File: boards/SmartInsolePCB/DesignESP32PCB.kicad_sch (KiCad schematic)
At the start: 48 parts, among them J1 Conn_01x02_Pin, J10 Conn_01x02_Pin, J11 Conn_01x02_Pin, J12 Conn_01x02_Pin, J2 Conn_01x02_Pin, J3 Conn_01x06_Pin, J4 Conn_01x02_Pin, J5 Conn_01x02_Pin, J6 Conn_01x02_Pin, J7 Conn_01x02_Pin, J8 Conn_01x02_Pin, J9 Conn_01x02_Pin, SW1 SW_Push, SW2 SW_Push, U2 D3V3XA4B10LP, U3 TLV75801PDRV, U6 MPU-6050, U7 ESP32-S3-WROOM-1

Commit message: finished schematic
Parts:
- removed BOOT1, RESET1: ~, Button_Switch_SMD:SW_Push_1P1T_NO_CK_PTS125Sx43PSMTR, symbol Switch:SW_MEC_5E
- removed J3: Conn_01x06_Pin, Connector_PinHeader_1.00mm:PinHeader_1x06_P1.00mm_Vertical, symbol Connector:Conn_01x06_Pin
- added J3: PJS008U-3000-0, SmartInsolePCB:PJS008U30000, symbol SD_Card_Connector:PJS008U-3000-0
- added SW3, SW4: SW_Push, Button_Switch_SMD:SW_Push_1P1T_NO_CK_PTS125Sx43PSMTR, symbol Switch:SW_Push
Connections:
- net GPIO10 is gone; now on net GPIO1: R3.1
- net GPIO13 is gone; now on net GPIO6: R11.1
- net GPIO14 is gone; now on net GPIO7: R12.1
- net GPIO15 is gone; now on net GPIO8: R13.1
- net GPIO16 is gone; now on net GPIO11: R18.1
- net GPIO17 is gone; now on net GPIO12: R19.1
- net GPIO18 is gone; now on net GPIO21: R20.1
- net GPIO19 is gone; now on net GPIO38: R21.1
- net GPIO20 is gone; now on net GPIO47: R22.1
- net SCK is gone; now on net GPIO11: U7.19 (IO11)
- net 3V3: now also J3.4
- net CS: now also U7.21 (IO13), J3.1; no longer U7.20 (IO12)
- net ESP32_EN: now also SW4.2
- net GND: now also J3.3, J3.6, SW3.1, SW4.1
- net GPIO0: now also SW3.2
- net GPIO11: no longer R9.1
- net GPIO12: now also U7.20 (IO12); no longer R10.1
- net MISO: now also U7.8 (IO15), J3.7; no longer U7.22 (IO14)
- net MOSI: now also U7.22 (IO14), J3.2; no longer U7.21 (IO13)
- net GPIO8: now reaches U7.12 (IO8)
- net GPIO3: now reaches U7.15 (IO3)
- net GPIO3: now also R10.1
- net GPIO21: now reaches U7.23 (IO21)
- net GPIO47: now reaches U7.24 (IO47)
- net GPIO38: now reaches U7.31 (IO38)
- net GPIO2: now reaches U7.38 (IO2)
- net GPIO2: now also R9.1
- net GPIO1: now reaches U7.39 (IO1)
- net GPIO6: now reaches U7.6 (IO6)
- net GPIO7: now reaches U7.7 (IO7)
- net SCLK: now reaches U7.9 (IO16)
- net SCLK: now also J3.5
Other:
- note added: "Buttons"
- note added: "ESP32"
- note added: "LDO"
- note added: "MPU 6050"
- note added: "SD Card"
- note added: "USB Connector"
- note added: "Velostat"
- note removed: "Attach to pins going to Velostat material"
- note removed: "Figure out how to interface with I2C and SD card"
- moved on the sheet: C1, C2, C3, C4, J1, J10, J11, J12, J2, J4, J5, J6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

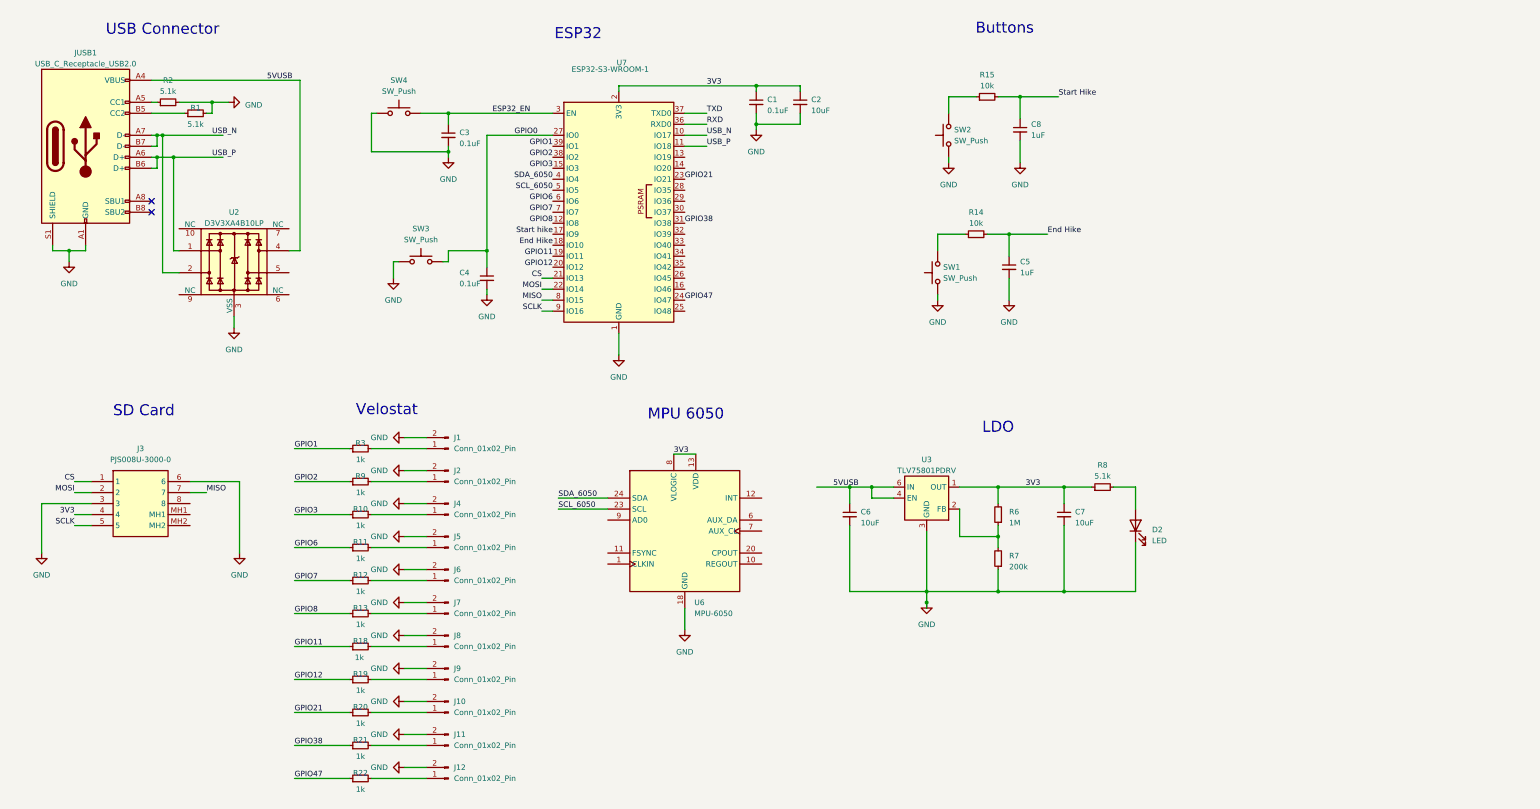
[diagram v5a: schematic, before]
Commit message: finished all PCB connections
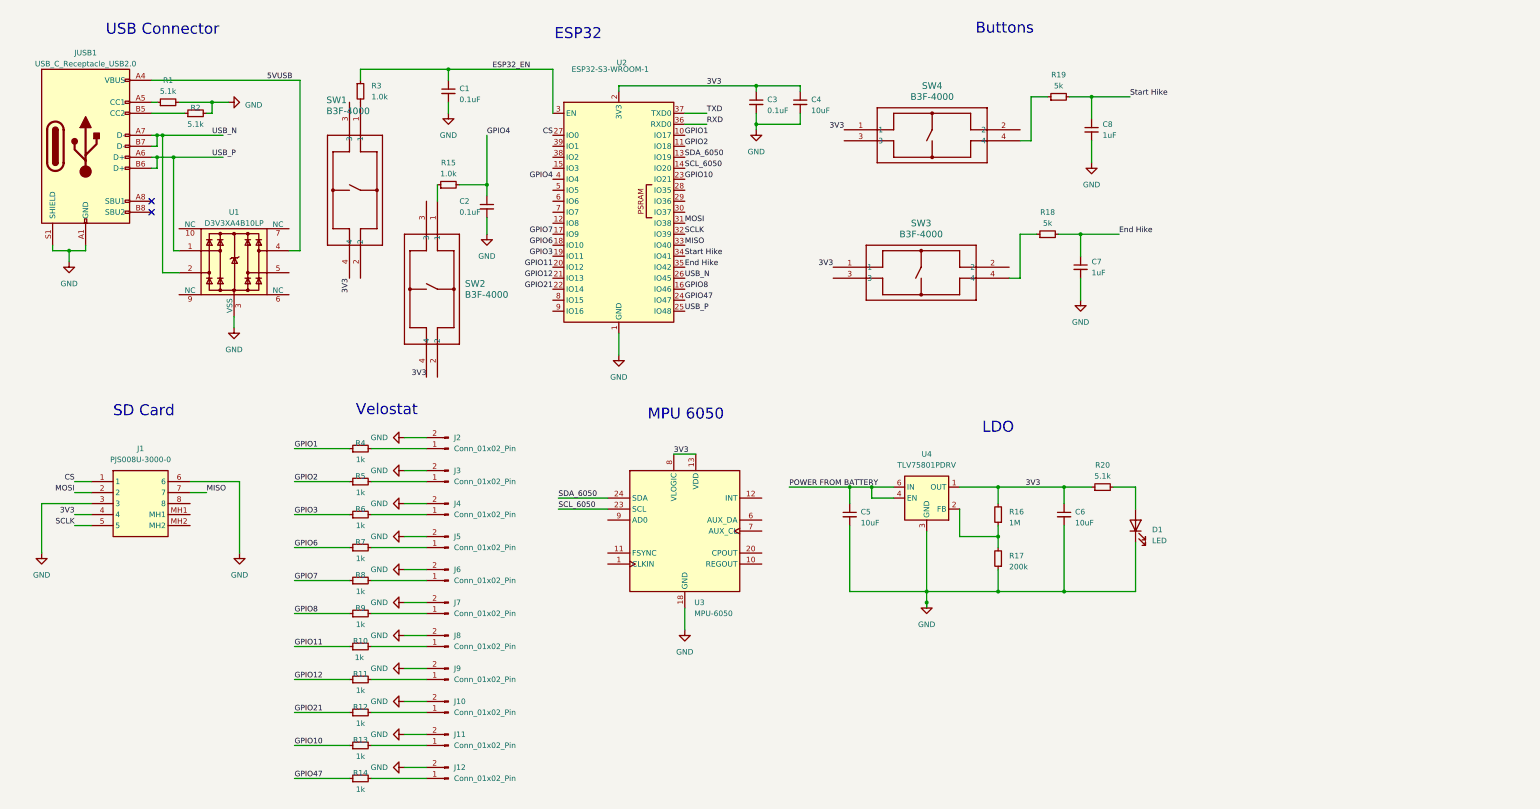
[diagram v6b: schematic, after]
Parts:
- removed SW1, SW2, SW3, SW4: SW_Push, Button_Switch_SMD:SW_Push_1P1T_NO_CK_PTS125Sx43PSMTR, symbol Switch:SW_Push
- added R15, R3: 1.0k, Resistor_SMD:R_0603_1608Metric, symbol Device:R_Small
- added SW1, SW2, SW3, SW4: B3F-4000, SmartInsolePCB:SW_B3F-4000_OMR, symbol SWITCH_TACTILE_SPST:B3F-4000
- R18: renamed from R14; value 10k -> 5k
- R19: renamed from R15; value 10k -> 5k
- renumbered C3 to C1, C4 to C2, C1 to C3, C2 to C4, C6 to C5, C7 to C6, C5 to C7, D2 to D1, J3 to J1, J1 to J2, J2 to J3, R2 to R1, R18 to R10, R19 to R11, R20 to R12, R21 to R13, R22 to R14, R6 to R16, R7 to R17, R1 to R2, R8 to R20, R3 to R4, R9 to R5, R10 to R6, R11 to R7, R12 to R8, R13 to R9, U2 to U1, U7 to U2, U6 to U3, U3 to U4
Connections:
- net Start hike is gone; now on net GPIO7: U2.17 (IO9)
- net 3V3: now also SW1.4, SW2.4, SW3.1, SW4.1
- net 5VUSB: no longer C5.1, U4.4 (EN), U4.6 (IN)
- net CS: now also U2.27 (IO0); no longer U2.21 (IO13)
- net ESP32_EN: now also R3.1
- net End Hike: now also U2.35 (IO42); no longer U2.18 (IO10)
- net GPIO1: now also U2.10 (IO17); no longer U2.39 (IO1)
- net GPIO11: now also U2.20 (IO12); no longer U2.19 (IO11)
- net GPIO12: now also U2.21 (IO13); no longer U2.20 (IO12)
- net GPIO2: now also U2.11 (IO18); no longer U2.38 (IO2)
- net GPIO21: now also U2.22 (IO14); no longer U2.23 (IO21)
- net GPIO3: now also U2.19 (IO11); no longer U2.15 (IO3)
- net GPIO6: now also U2.18 (IO10); no longer U2.6 (IO6)
- net GPIO7: no longer U2.7 (IO7)
- net GPIO8: now also U2.16 (IO46); no longer U2.12 (IO8)
- net MISO: now also U2.33 (IO40); no longer U2.8 (IO15)
- net MOSI: now also U2.31 (IO38); no longer U2.22 (IO14)
- net SCLK: now also U2.32 (IO39); no longer U2.9 (IO16)
- net SCL_6050: now also U2.14 (IO20); no longer U2.5 (IO5)
- net SDA_6050: now also U2.13 (IO19); no longer U2.4 (IO4)
- net Start Hike: now also U2.34 (IO41)
- net USB_N: now also U2.26 (IO45); no longer U2.10 (IO17)
- net USB_P: now also U2.25 (IO48); no longer U2.11 (IO18)
- net at R19.1: now also SW4.4
- net at R18.1: now also SW3.4
- net GPIO0 renamed GPIO4
- net GPIO4: now also U2.4 (IO4), R15.2; no longer U2.27 (IO0)
- net GPIO38 renamed GPIO10
- net GPIO10: now also U2.23 (IO21); no longer U2.31 (IO38)
- new net: R15.1, SW2.1
- new net: R3.2, SW1.1
- new net POWER FROM BATTERY: C5.1, U4.4 (EN), U4.6 (IN)
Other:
- moved on the sheet: C1, C2, C7, C8, R18, R19

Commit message: changed GPIO
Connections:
- net CS: now also U2.21 (IO13); no longer U2.27 (IO0)
- net GPIO12: now also U2.7 (IO7); no longer U2.21 (IO13)
- net GPIO21: now also U2.12 (IO8); no longer U2.22 (IO14)
- net MISO: now also U2.9 (IO16); no longer U2.33 (IO40)
- net MOSI: now also U2.22 (IO14); no longer U2.31 (IO38)
- net SCLK: now also U2.8 (IO15); no longer U2.32 (IO39)
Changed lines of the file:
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@@
 	)
 	(label "MOSI"
-		(at 168.91 63.5 0)
-		(fields_autoplaced yes)
-		(effects
-			(font
-				(size 1.27 1.27)
-			)
-			(justify left bottom)
+		(at 138.43 78.74 180)
+		(fields_autoplaced yes)
+		(effects
+			(font
+				(size 1.27 1.27)
+			)
+			(justify right bottom)
 		)
 	)
@@
 	)
 	(label "GPIO21"
-		(at 138.43 78.74 180)
+		(at 138.43 63.5 180)
 		(fields_autoplaced yes)
 		(effects
@@
 	)
 	(label "MISO"
-		(at 168.91 68.58 0)
-		(fields_autoplaced yes)
-		(effects
-			(font
-				(size 1.27 1.27)
-			)
-			(justify left bottom)
+		(at 138.43 83.82 180)
+		(fields_autoplaced yes)
+		(effects
+			(font
+				(size 1.27 1.27)
+			)
+			(justify right bottom)
 		)
 	)
@@
 	)
 	(label "GPIO12"
-		(at 138.43 76.2 180)
+		(at 138.43 60.96 180)
 		(fields_autoplaced yes)
 		(effects
@@
 	)
 	(label "CS"
-		(at 138.43 43.18 180)
+		(at 138.43 76.2 180)
 		(fields_autoplaced yes)
 		(effects
@@
 	)
 	(label "SCLK"
-		(at 168.91 66.04 0)
-		(fields_autoplaced yes)
-		(effects
-			(font
-				(size 1.27 1.27)
-			)
-			(justify left bottom)
-		)
-	)
+		(at 138.43 81.28 180)
+		(fields_autoplaced yes)
+		(effects
+			(font
+				(size 1.27 1.27)
+			)
+			(justify right bottom)
+		)
+	)

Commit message: schematic and pcb updates
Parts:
- removed U2: ESP32-S3-WROOM-1, RF_Module:ESP32-S3-WROOM-1, symbol RF_Module:ESP32-S3-WROOM-1
- added J13: Conn_01x05_Socket, Connector_PinHeader_1.00mm:PinHeader_1x05_P1.00mm_Vertical_SMD_Pin1Left, symbol Connector:Conn_01x05_Socket
- added JP1: SolderJumper_3_Open, Jumper:SolderJumper-3_P2.0mm_Open_TrianglePad1.0x1.5mm, symbol Jumper:SolderJumper_3_Open
- added Q1, Q2: SS8050-G, SmartInsolePCB:TRAN_SS8050-G_CIP, symbol NPN_BJT:SS8050-G
- added R21: 1.0k, Resistor_SMD:R_0603_1608Metric, symbol Device:R_Small
- added R22: 1k, Resistor_SMD:R_0603_1608Metric, symbol Device:R_Small
- added R23, R24, R25, R26: 10k, Resistor_SMD:R_0603_1608Metric, symbol Device:R_Small
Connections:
- net SDA_6050 is gone; now on net SCL_6050: U3.24 (SDA)
- net 3V3: now also R10.2, R11.2, R12.2, R13.2, R14.2, R15.2, R3.2, R4.2, R5.2, R6.2, R7.2, R8.2, R9.2, JP1.3 (B), R21.2; no longer SW1.4, SW2.4
- net ESP32_EN: now also SW1.4, R24.2; no longer C1.1
- net GND: now also SW1.1, SW2.1, J13.5 (Pin_5), JP1.1 (A)
- net GPIO1: now also J2.1 (Pin_1)
- net GPIO10: now also J11.1 (Pin_1)
- net GPIO11: now also J8.1 (Pin_1)
- net GPIO12: now also J9.1 (Pin_1)
- net GPIO2: now also J3.1 (Pin_1)
- net GPIO21: now also J10.1 (Pin_1)
- net GPIO3: now also J4.1 (Pin_1)
- net GPIO47: now also J12.1 (Pin_1)
- net GPIO6: now also J5.1 (Pin_1)
- net GPIO7: now also J6.1 (Pin_1)
- net GPIO8: now also J7.1 (Pin_1)
- net SCL_6050: now also U3.9 (AD0)
- net GPIO0_STRAPPING: now reaches R15.1
- net GPIO0_STRAPPING: now also SW2.4, R26.2; no longer SW2.1
- net at SW2.3: now also C2.1
- net at SW1.3: now also C1.1
- removed net GPIO4: C2.1, R15.2
- new net: Q1.3, R24.1
- new net: Q1.1, R23.2
- new net: Q2.1, R25.2
- new net: Q2.3, R26.1
- new net: JP1.2 (C), R22.1
- new net DTR: J13.2 (Pin_2), Q2.2, R23.1
- new net GPIO3_STRAPPING: R22.2
- new net GPIO46_STRAPPING: R21.1
- new net RTS: J13.1 (Pin_1), Q1.2, R25.1
- new net RX: J13.4 (Pin_4)
- new net TX: J13.3 (Pin_3)
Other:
- moved on the sheet: J1, J10, J11, J12, J2, J3, J4, J5, J6, J7, J8, J9
